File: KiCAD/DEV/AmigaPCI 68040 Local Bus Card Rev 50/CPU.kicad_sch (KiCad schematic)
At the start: 22 parts, among them J100 SNOOP, U200 MC68040, U203 74LVC245

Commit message: CPU Card Rev 5.0 - Connect _MI to U400.
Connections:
- net GND: now also U200.148 (TCK), U200.170 (DLE)
- net _MI: now reaches U200.124 (_MI)
- no-connect marks 23 -> 20
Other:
- moved on the sheet: R105, R110

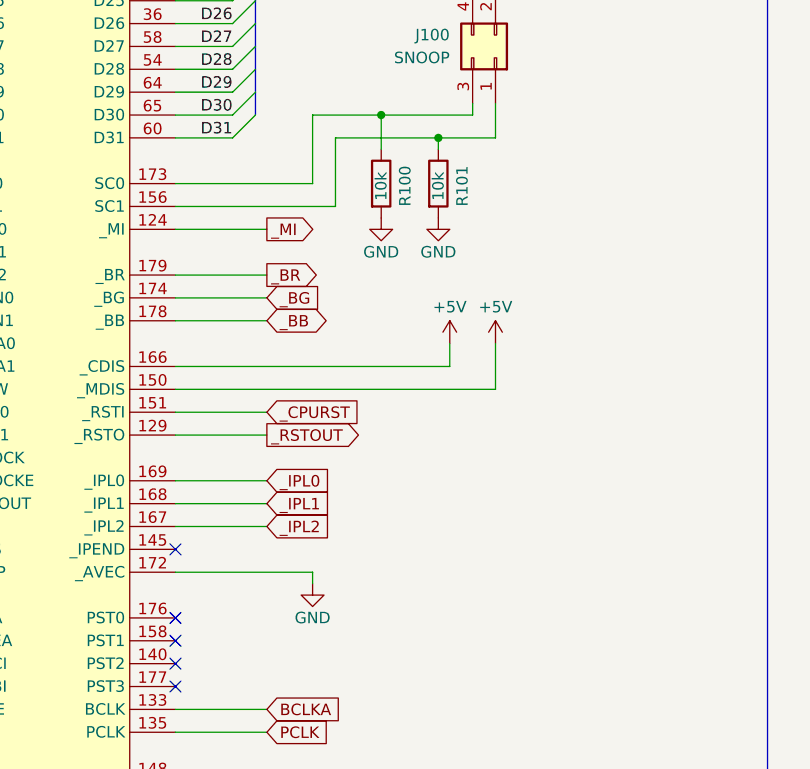
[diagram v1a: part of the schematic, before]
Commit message: Local Bus 68040 Card Rev 5.0 Work
Added jumper to disable MMU and Cache for troubleshooting.
Updated design date.
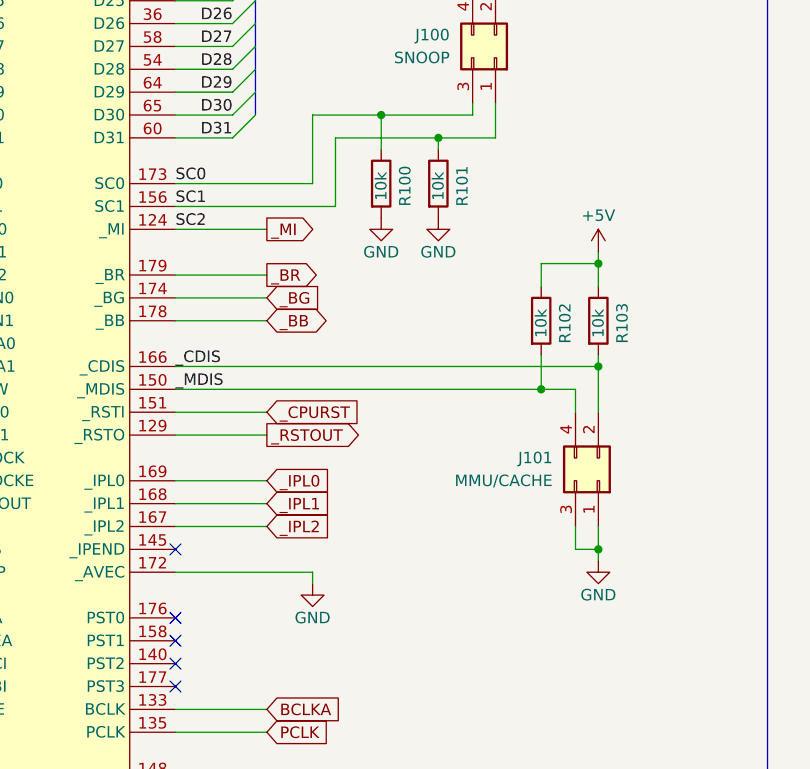
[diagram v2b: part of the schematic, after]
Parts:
- added J101: MMU/CACHE, Connector_PinHeader_2.54mm:PinHeader_2x02_P2.54mm_Vertical, symbol Connector_Generic:Conn_02x02_Odd_Even
- added R102, R103: 10k, Resistor_SMD:R_0603_1608Metric, symbol Device:R
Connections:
- net +5V: now also R102.1, R103.1; no longer U200.150 (_MDIS), U200.166 (_CDIS)
- net GND: now also J101.1 (Pin_1), J101.3 (Pin_3)
- net SC1: now reaches J100.1 (Pin_1), R101.1, U200.156 (SC1)
- net SC0: now reaches J100.3 (Pin_3), R100.1, U200.173 (SC0)
- new net _CDIS: J101.2 (Pin_2), R103.2, U200.166 (_CDIS)
- new net _MDIS: J101.4 (Pin_4), R102.2, U200.150 (_MDIS)
